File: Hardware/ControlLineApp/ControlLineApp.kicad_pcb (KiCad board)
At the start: 2 copper layers, 63 x 29 mm, 13 parts, among them J2 

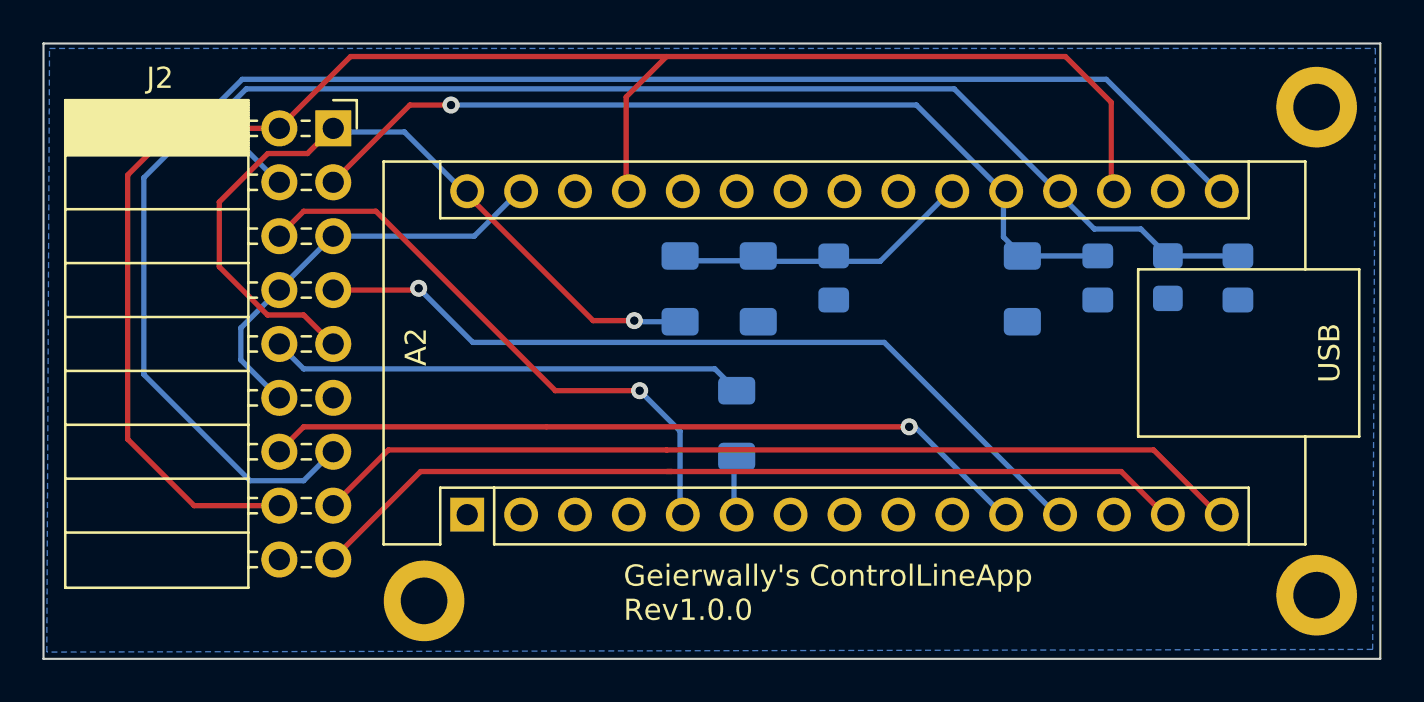
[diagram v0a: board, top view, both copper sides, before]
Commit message: PCB and schematic adapted with I²C interface, software implementation accelerometer gyroscope
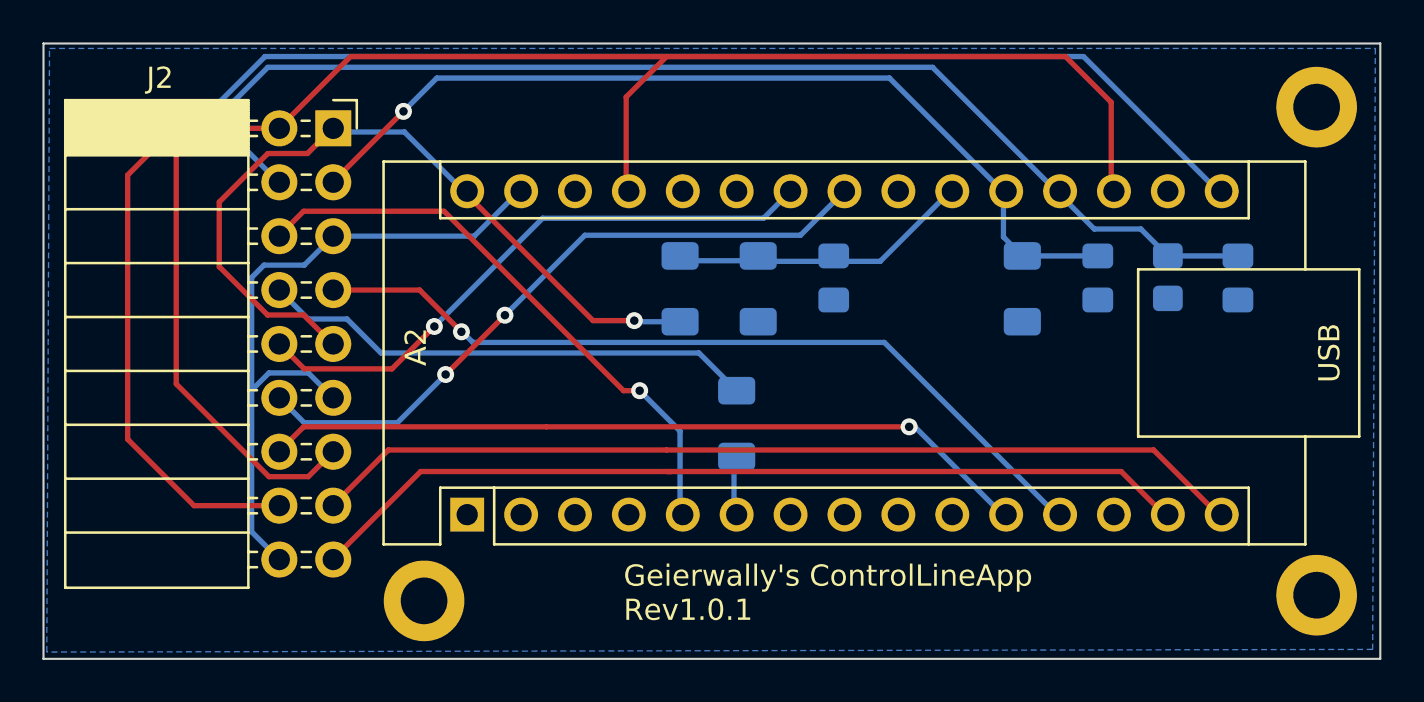
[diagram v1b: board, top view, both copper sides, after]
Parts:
- A2: value (none) -> Arduino Nano
- J2: value (none) -> Conn_02x09
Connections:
- A2 pad 23: unconnected-(A2-SDA/A4-Pad23) -> SDA
- A2 pad 24: unconnected-(A2-SCL/A5-Pad24) -> SCL
- J2 pad 10: LED_A -> SCL
- J2 pad 12: GNDREF -> SDA
- J2 pad 8: GNDREF -> LED_A
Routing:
- net SDA: track 0.00 -> 31.6 mm, vias 0 -> 2
- net SCL: track 0.00 -> 28.0 mm, vias 0 -> 1
- net GNDREF: track 19.8 -> 32.8 mm
- net SCK_SPI: track 75.6 -> 74.5 mm, vias 0 -> 1
- net VPCell_1: track 41.8 -> 42.8 mm
- net LED_A: track 22.5 -> 23.5 mm
- net Poti10K: track 55.7 -> 56.5 mm
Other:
- board text added: "Geierwally's ControlLineApp Rev1.0.1"
- board text removed: "Geierwally's ControlLineApp Rev1.0.0"

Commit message: App extended with additional functions like retractable landing gear
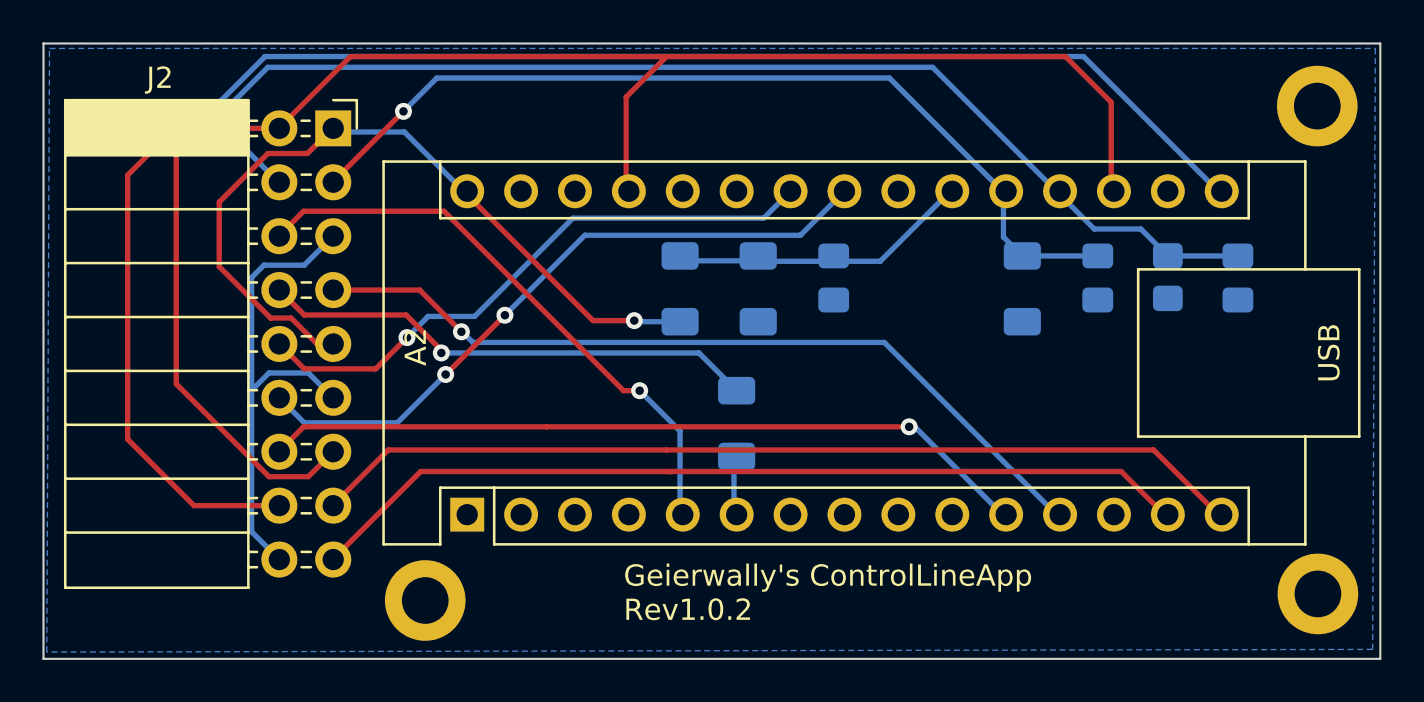
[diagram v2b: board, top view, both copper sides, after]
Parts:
- removed  : , MountingHole:MountingHole_2.2mm_M2_DIN965_Pad (x3)
- added H1: MountingHole_Pad, MountingHole:MountingHole_2.2mm_M2_DIN965_Pad, F.Cu at (165.0, 89.0)
- added H2: MountingHole_Pad, MountingHole:MountingHole_2.2mm_M2_DIN965_Pad, F.Cu at (165.1, 111.9)
- added H3: MountingHole_Pad, MountingHole:MountingHole_2.2mm_M2_DIN965_Pad, F.Cu at (123.0, 112.2)
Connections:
- net MISO_SPI renamed D12_FunctionPin4
- net MOSI_SPI renamed PWM RetractLandingGear
- net SCK_SPI renamed D13_FunctionPin5
- net SS_SPI renamed D8_FunctionPin3
- net ServoPulse renamed PWM Throttle
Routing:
- net GNDREF: track 32.8 -> 23.2 mm
- net LED_A: track 23.5 -> 23.6 mm, vias 0 -> 1
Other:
- board text added: "Geierwally's ControlLineApp Rev1.0.2"
